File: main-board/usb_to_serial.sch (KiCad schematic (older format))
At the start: 20 parts, among them J201 C10418, Q201 Q_NPN_BCE, Q202 Q_NPN_BCE, U201 HT7333-A, U202 CH340E

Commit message: ALPHA 1
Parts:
- added TP201: +5V, TestPoint:TestPoint_Pad_D1.0mm, symbol Connector:TestPoint
- added TP202: +3.3V, TestPoint:TestPoint_Pad_D1.0mm, symbol Connector:TestPoint
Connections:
- wire segments 63 -> 65
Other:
- moved on the sheet: C201, C202, C203, C204, D201, D202, D203, D204, F201, J201, Q201, Q202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

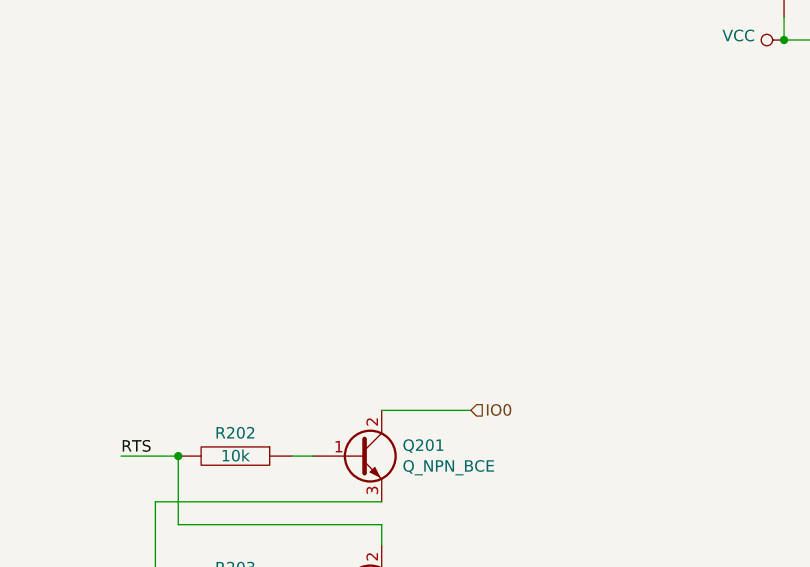
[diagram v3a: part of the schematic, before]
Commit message: added battery charging
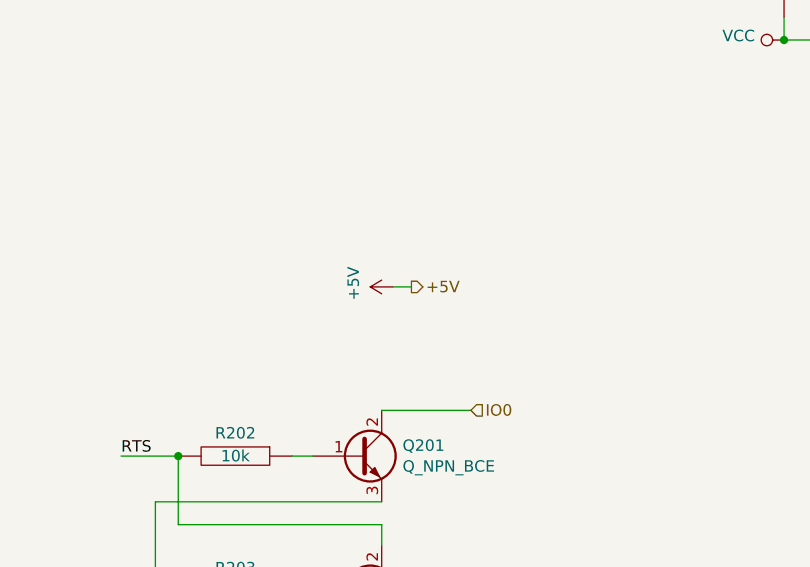
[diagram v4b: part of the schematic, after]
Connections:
- wire segments 65 -> 66
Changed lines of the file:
@@
 $EndComp
 $Comp
-L power:GND #PWR0215
+L power:GND #PWR0216
 U 1 1 5DB4F803
 P 8930 4890
-F 0 "#PWR0215" H 8930 4640 50  0001 C CNN
+F 0 "#PWR0216" H 8930 4640 50  0001 C CNN
 F 1 "GND" H 8935 4717 50  0000 C CNN
 F 2 "" H 8930 4890 50  0001 C CNN
@@
 D-
 $Comp
-L power:GND #PWR0214
+L power:GND #PWR0215
 U 1 1 5DB4F810
 P 8230 3900
-F 0 "#PWR0214" H 8230 3650 50  0001 C CNN
+F 0 "#PWR0215" H 8230 3650 50  0001 C CNN
 F 1 "GND" H 8235 3727 50  0000 C CNN
 F 2 "" H 8230 3900 50  0001 C CNN
@@
 	7580 3500 8230 3500
 $Comp
-L power:GND #PWR0212
+L power:GND #PWR0213
 U 1 1 5DB4F82B
 P 8130 2850
-F 0 "#PWR0212" H 8130 2600 50  0001 C CNN
+F 0 "#PWR0213" H 8130 2600 50  0001 C CNN
 F 1 "GND" H 8135 2677 50  0000 C CNN
 F 2 "" H 8130 2850 50  0001 C CNN
@@
 $EndComp
 $Comp
-L power:GND #PWR0210
+L power:GND #PWR0211
 U 1 1 5DB4F831
 P 7580 3050
-F 0 "#PWR0210" H 7580 2800 50  0001 C CNN
+F 0 "#PWR0211" H 7580 2800 50  0001 C CNN
 F 1 "GND" H 7585 2877 50  0000 C CNN
 F 2 "" H 7580 3050 50  0001 C CNN
@@
 Connection ~ 9680 3400
 $Comp
-L power:VCC #PWR0213
+L power:VCC #PWR0214
 U 1 1 5DB4F865
 P 8130 3400
-F 0 "#PWR0213" H 8130 3250 50  0001 C CNN
+F 0 "#PWR0214" H 8130 3250 50  0001 C CNN
 F 1 "VCC" V 8130 3520 50  0000 L CNN
 F 2 "" H 8130 3400 50  0001 C CNN
@@
 Connection ~ 8130 3400
 $Comp
-L power:VCC #PWR0211
+L power:VCC #PWR0212
 U 1 1 5DB4F86C
 P 7580 3500
-F 0 "#PWR0211" H 7580 3350 50  0001 C CNN
+F 0 "#PWR0212" H 7580 3350 50  0001 C CNN
 F 1 "VCC" V 7598 3627 50  0000 L CNN
 F 2 "" H 7580 3500 50  0001 C CNN
@@
 Connection ~ 7580 3500
 $Comp
-L power:VCC #PWR0216
+L power:VCC #PWR0217
 U 1 1 5DB4F873
 P 9180 2750
-F 0 "#PWR0216" H 9180 2600 50  0001 C CNN
+F 0 "#PWR0217" H 9180 2600 50  0001 C CNN
 F 1 "VCC" V 9198 2877 50  0000 L CNN
 F 2 "" H 9180 2750 50  0001 C CNN
@@
 TNOW
 $Comp
-L power:VCC #PWR0217
+L power:VCC #PWR0218
 U 1 1 5DB4F879
 P 10090 4300
-F 0 "#PWR0217" H 10090 4150 50  0001 C CNN
+F 0 "#PWR0218" H 10090 4150 50  0001 C CNN
 F 1 "VCC" V 10108 4427 50  0000 L CNN
 F 2 "" H 10090 4300 50  0001 C CNN
@@
 Wire Wire Line
 	1450 5770 1520 5770
+Text HLabel 5950 4580 2    50   Output ~ 0
++5V
+$Comp
+L power:+5V #PWR?
+U 1 1 5DB86DF2
+P 5870 4580
+AR Path="/5DB86DF2" Ref="#PWR?"  Part="1"
+AR Path="/5DA658CB/5DB86DF2" Ref="#PWR0210"  Part="1"
+F 0 "#PWR0210" H 5870 4430 50  0001 C CNN
+F 1 "+5V" H 5885 4753 50  0000 C CNN
+F 2 "" H 5870 4580 50  0001 C CNN
+F 3 "" H 5870 4580 50  0001 C CNN
+	1    5870 4580
+	0    -1   -1   0
+$EndComp
+Wire Wire Line
+	5870 4580 5950 4580
 $EndSCHEMATC
